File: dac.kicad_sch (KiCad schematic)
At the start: 65 parts

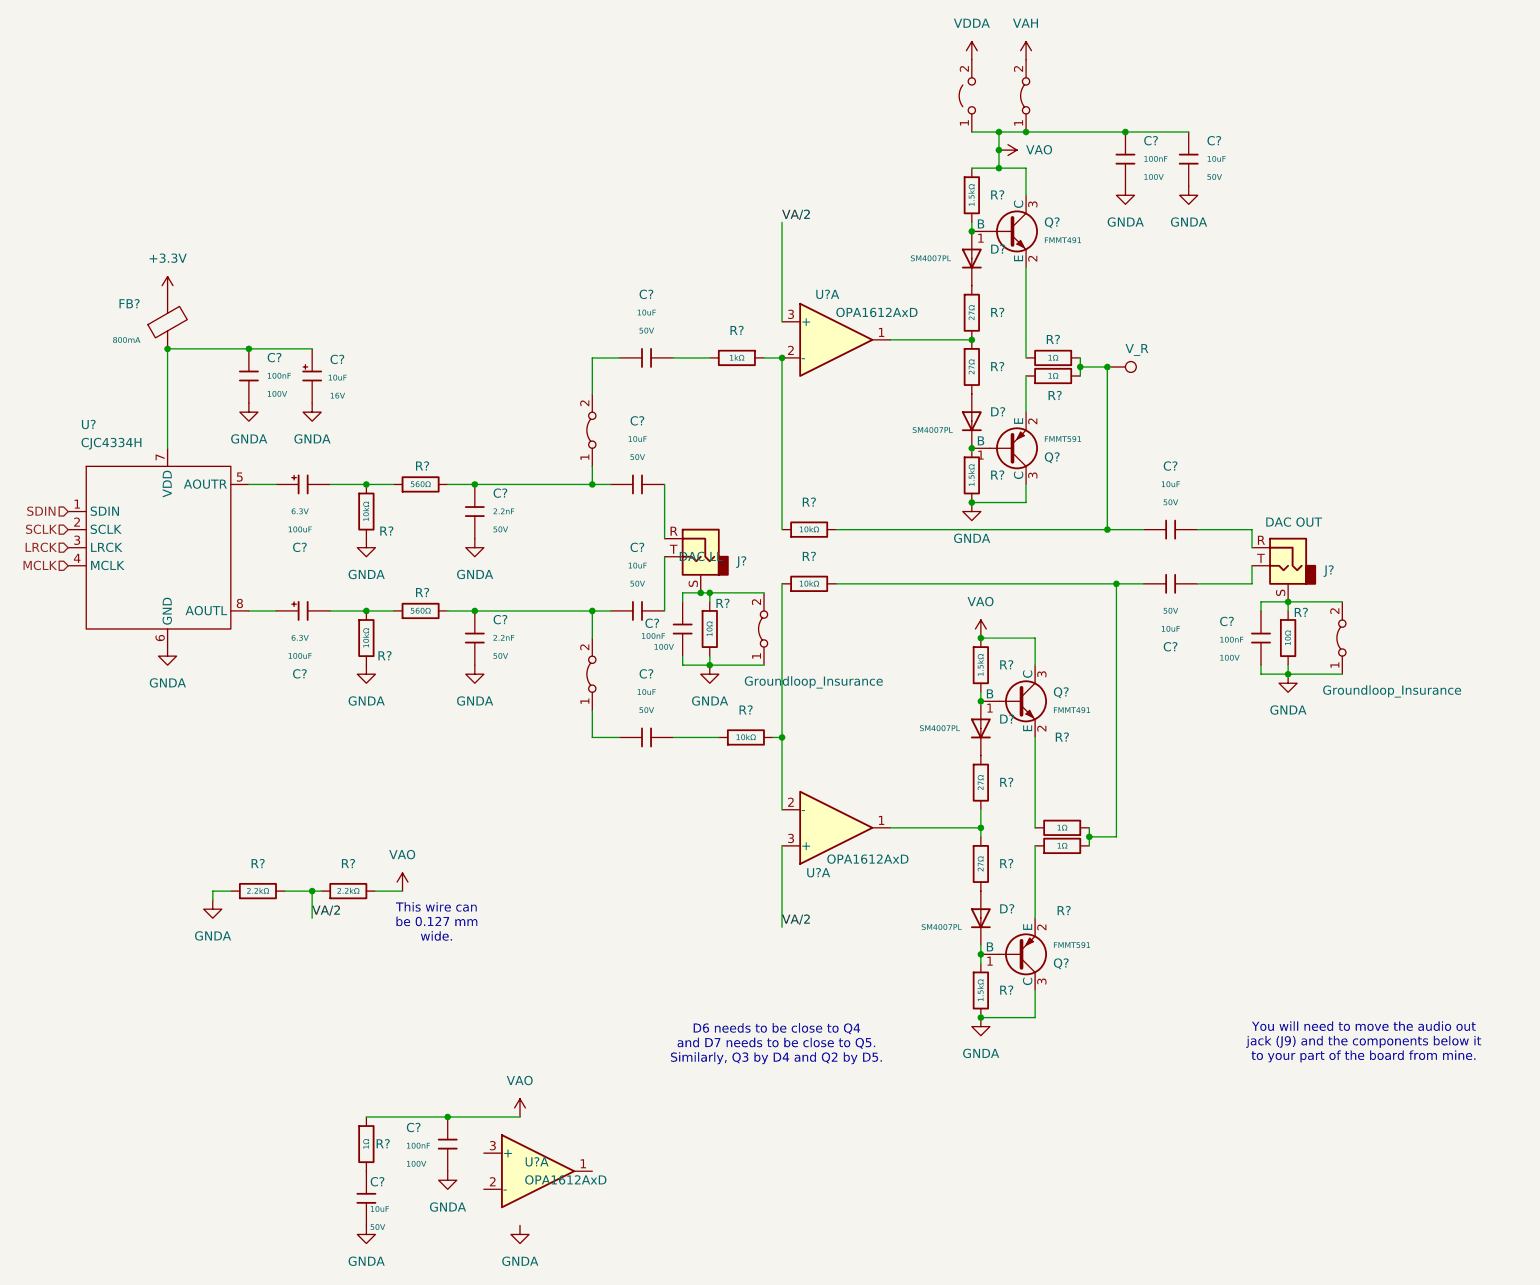
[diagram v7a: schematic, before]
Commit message: Initial v0.2
Fixed SCL-SDA swap, 3V3 on encoder, and 3D models for Kicad 10
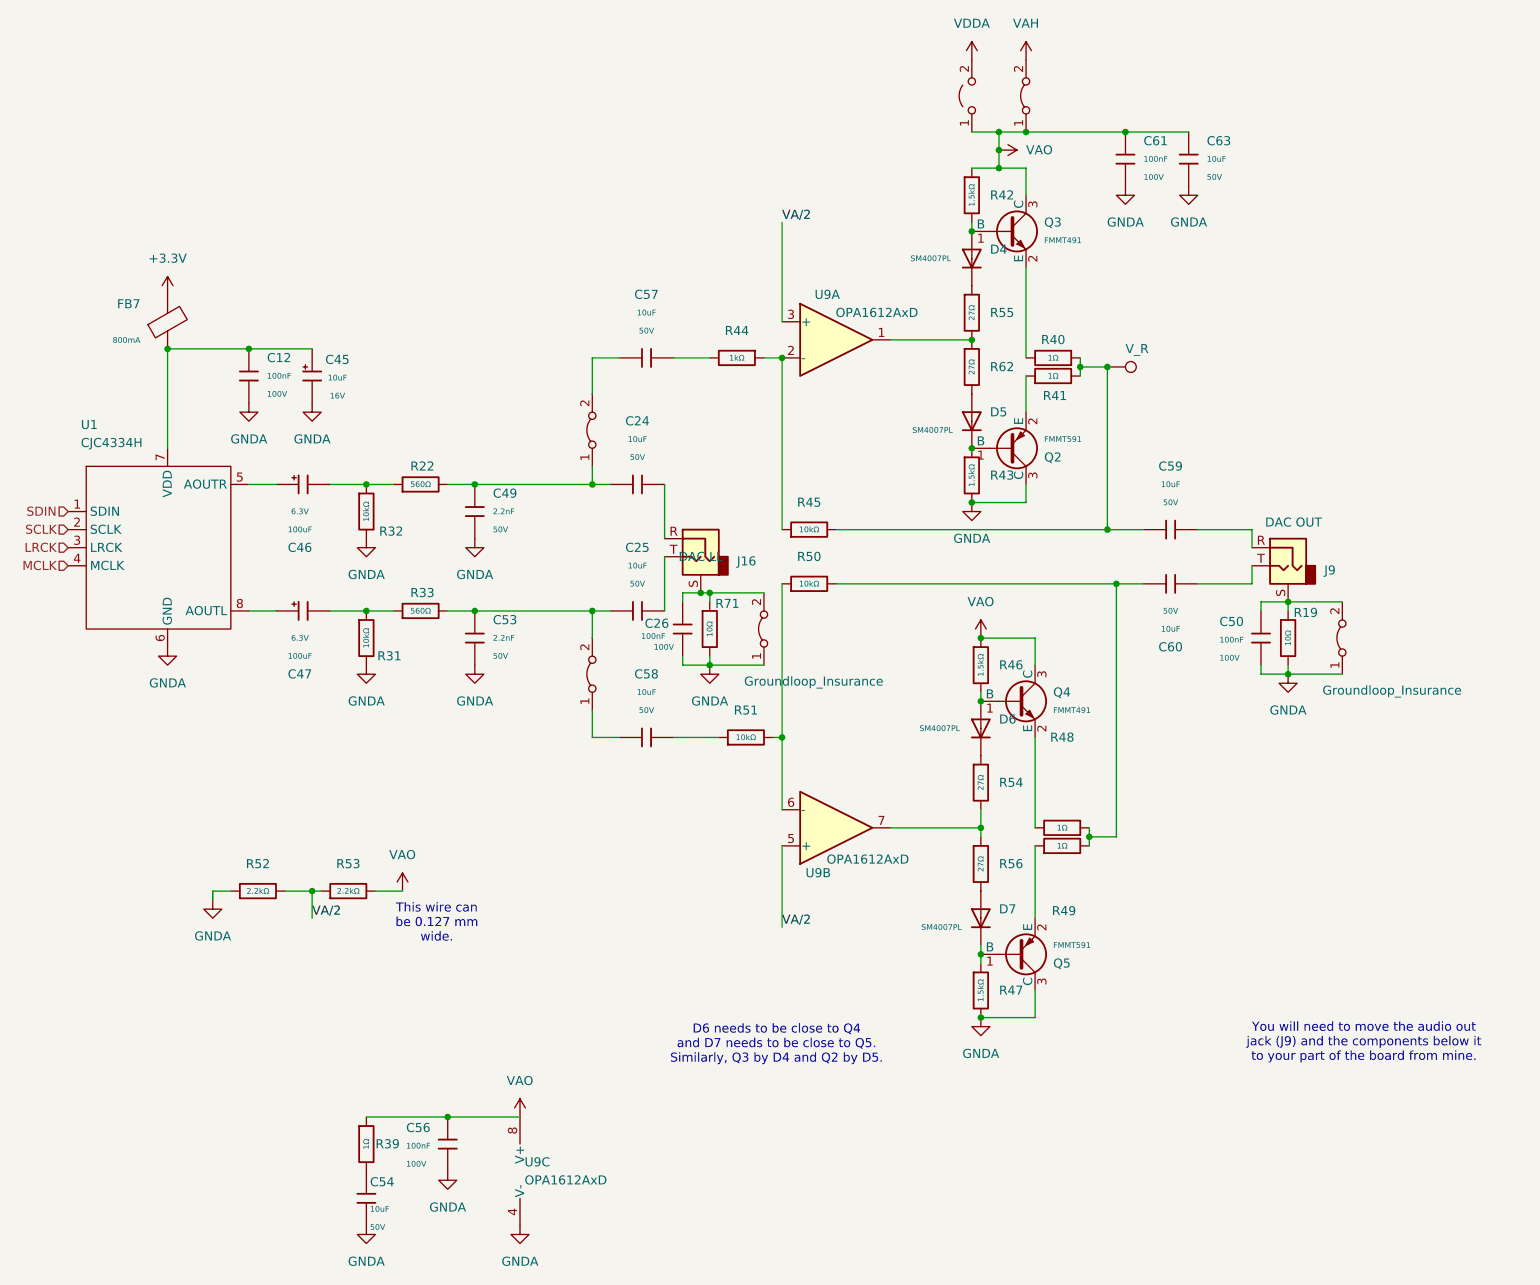
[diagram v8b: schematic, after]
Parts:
- FB7: renamed from FB?; value ~ -> (none)
- JP3: renamed from JP?; value ~ -> (none)
- e2, e6, e7: renamed from e?; value ~ -> (none)
- gave numbers to parts that had none: 58
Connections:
- net GNDA: now also U9.4 (V-)
- net VAO: now also U9.8 (V+)
- net VA/2: now also U9.5 (+); no longer U9.3 (+)
- net at R54.2, R56.1: now also U9.7; no longer U9.1
- net at R50.1, R51.2: now also U9.6 (-); no longer U9.2 (-)
